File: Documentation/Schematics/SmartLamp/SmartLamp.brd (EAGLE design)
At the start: 53.3 x 51.8 mm, 31 parts, among them J1 POWER_JACKPTH_BREAD, J2 AVR_SPI_PROG_5X2PTH2, Q1 STN4NF03L, Q2 STN4NF03L, Q3 STN4NF03L, U1 MIC2920A, U2 DS3231MZ, U3 ATMEGA8/168/328, U4 HM-10

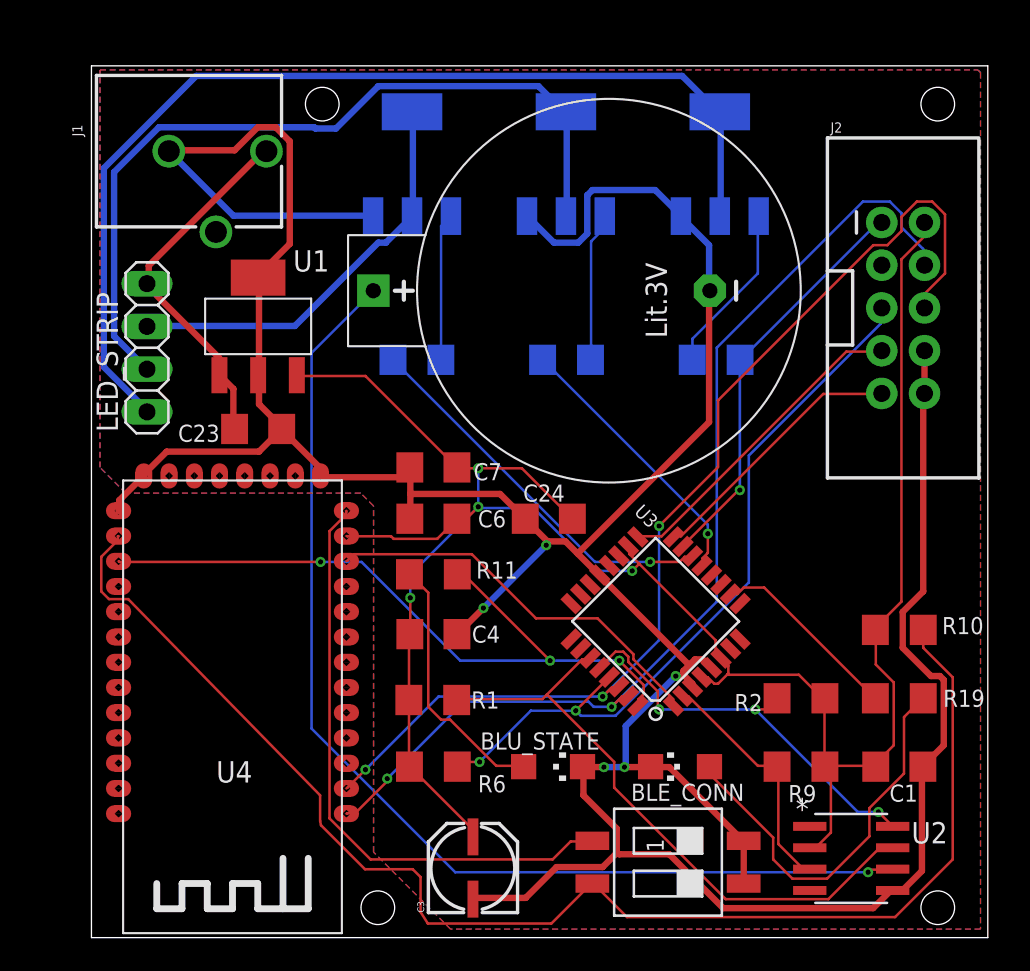
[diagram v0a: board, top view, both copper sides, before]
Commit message: Fixed DC jack and battery holder footprint.. milling level needed for slot holes.
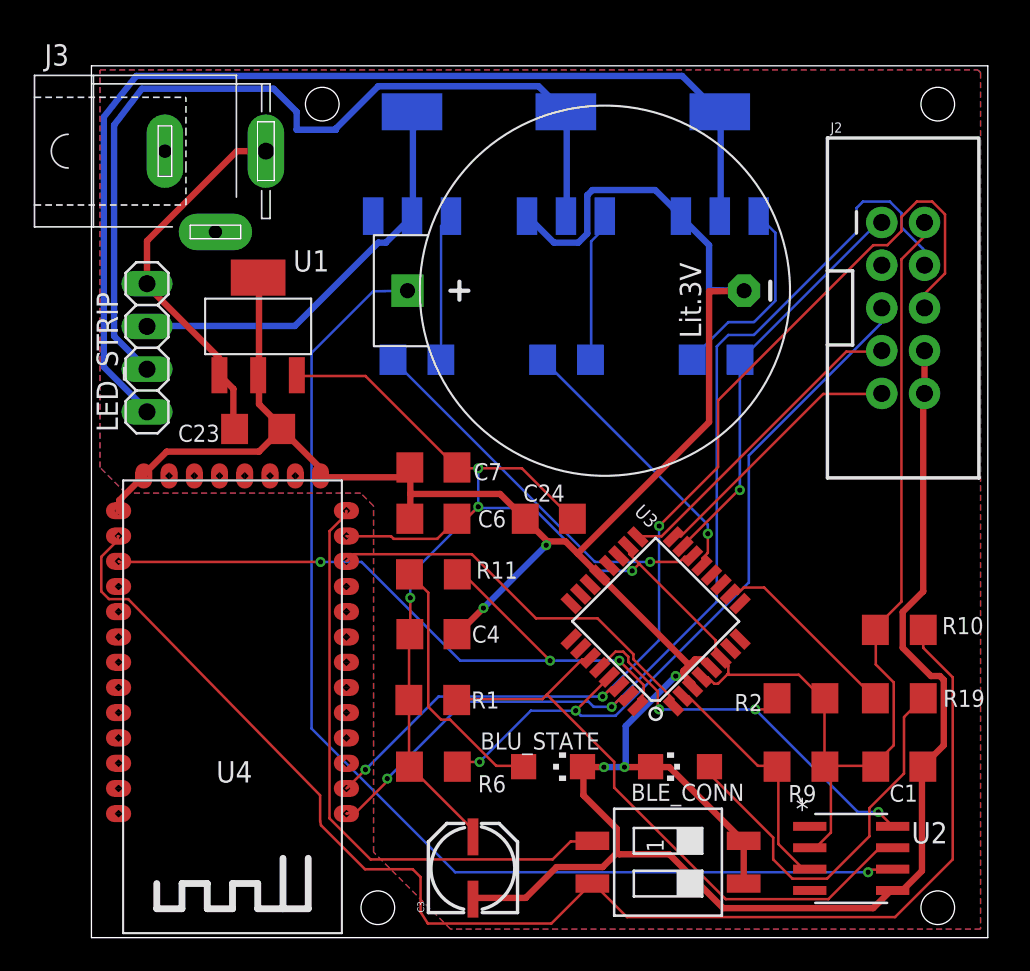
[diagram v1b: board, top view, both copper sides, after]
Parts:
- removed J1: POWER_JACKPTH_BREAD, SparkFun-Connectors:POWER_JACK_PTH_BREAD
- added J3: (no value), con-jack:SPC4077
- G1: value CR2032_EBM -> CR2032AMAZON; device CuSTOM_GB:CR2032_EBM -> CuSTOM_GB:CR2032_AMAZON
- moved G1 2.03 mm to (33.0, 38.4)
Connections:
- net +12V: now also J3.3; no longer J1.PWR
- net GND: now also J3.1; no longer J1.GND
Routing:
- net GND: track 224.4 -> 197.7 mm
- net RED_12V: track 48.4 -> 52.9 mm
- net VBAT: track 65.7 -> 67.7 mm
- net BLUE_12V: track 61.6 -> 63.5 mm
- net N$11: track 10.2 -> 11.9 mm
- net +12V: track 21.7 -> 22.6 mm
- net S_IN: track 62.4 -> 63.3 mm
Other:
- board text added: "SmartLamp SMD v1.1"
- board text removed: "SmartLamp SMD v1.0"

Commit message: Fixed GND - switch connection for HM-10
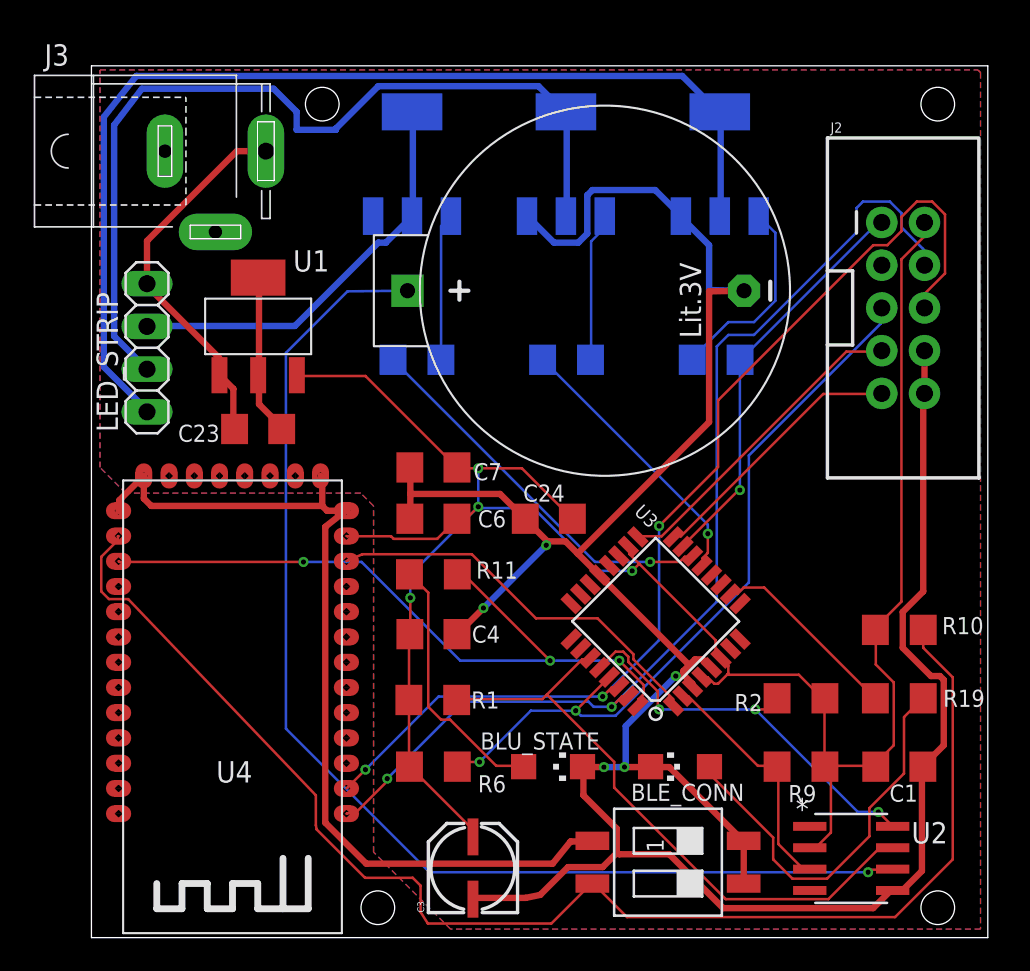
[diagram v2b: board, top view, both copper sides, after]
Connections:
- removed net BLU_SWITCH: S1.1, U4.13
- new net BLU_GND: S1.1, U4.13, U4.14, U4.21, U4.22
- net GND: no longer U4.14, U4.21, U4.22
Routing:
- net BLU_GND: track 0.00 -> 55.0 mm
- net BLU_SWITCH: track 35.8 -> 0.00 mm
- net GND: track 197.7 -> 176.1 mm
- net VBAT: track 67.7 -> 70.7 mm

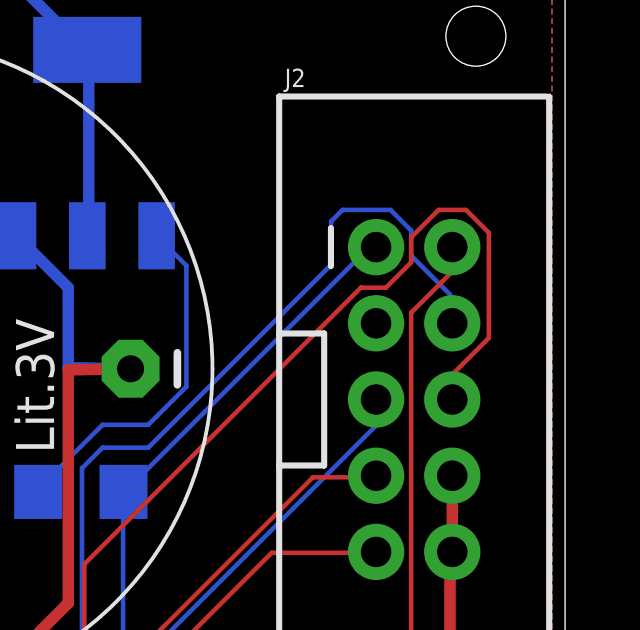
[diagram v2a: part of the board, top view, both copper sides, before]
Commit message: Fixed TX and RX swapped on PCB...
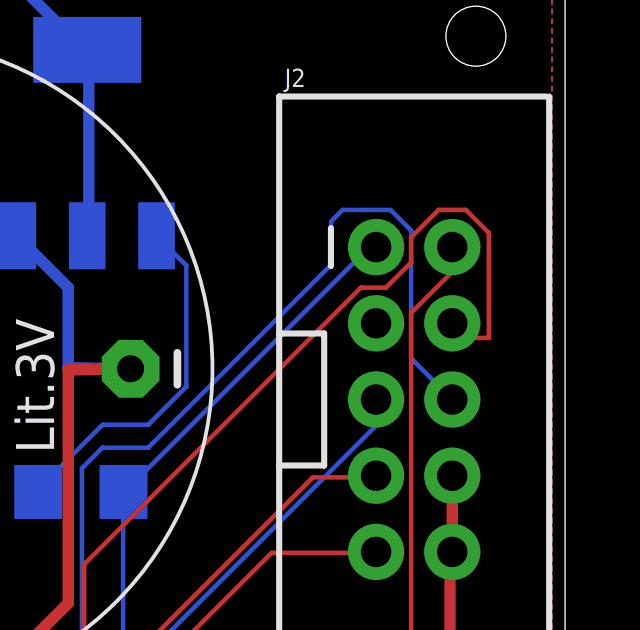
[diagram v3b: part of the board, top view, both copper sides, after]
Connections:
- net S_IN: now also J2.6; no longer J2.4
- net S_OUT: now also J2.4; no longer J2.6
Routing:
- net S_IN: track 63.3 -> 65.9 mm
- net S_OUT: track 64.4 -> 63.5 mm
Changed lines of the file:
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@@
 <contactref element="U4" pad="2"/>
 <contactref element="U3" pad="30"/>
-<contactref element="J2" pad="6"/>
 <wire x1="31.1658" y1="14.859" x2="31.5468" y2="14.859" width="0.1524" layer="1"/>
 <wire x1="30.6324" y1="14.3256" x2="31.1658" y2="14.859" width="0.1524" layer="1"/>
@@
 <wire x1="31.5468" y1="14.859" x2="31.5952" y2="14.91214375" width="0.1524" layer="1"/>
 <wire x1="15.4686" y1="8.9154" x2="15.406" y2="8.866" width="0.1524" layer="1"/>
-<wire x1="49.7586" y1="38.2524" x2="49.7586" y2="37.4904" width="0.1524" layer="1"/>
-<wire x1="50.9778" y1="39.4716" x2="49.7586" y2="38.2524" width="0.1524" layer="1"/>
 <wire x1="50.9778" y1="42.9768" x2="50.9778" y2="39.4716" width="0.1524" layer="1"/>
 <wire x1="50.2158" y1="43.7388" x2="50.9778" y2="42.9768" width="0.1524" layer="1"/>
@@
 <wire x1="33.9852" y1="17.6784" x2="33.9852" y2="24.4602" width="0.1524" layer="16"/>
 <wire x1="30.6324" y1="14.3256" x2="33.9852" y2="17.6784" width="0.1524" layer="16"/>
-<wire x1="49.7586" y1="37.4904" x2="49.758596875" y2="37.41928125" width="0.1524" layer="1"/>
 <via x="30.6324" y="14.3256" extent="1-16" drill="0.3048"/>
 <via x="16.5354" y="9.9822" extent="1-16" drill="0.3048"/>
 <via x="33.9852" y="24.4602" extent="1-16" drill="0.3048"/>
+<contactref element="J2" pad="4"/>
+<wire x1="50.9778" y1="39.4716" x2="49.758596875" y2="39.4716" width="0.1524" layer="1"/>
+<wire x1="49.758596875" y1="39.4716" x2="49.758596875" y2="39.95928125" width="0.1524" layer="1"/>
 </signal>
 <signal name="S_IN">
 <contactref element="U4" pad="1"/>
 <contactref element="U3" pad="31"/>
-<contactref element="J2" pad="4"/>
 <wire x1="31.7754" y1="14.3256" x2="32.1564" y2="14.3256" width="0.1524" layer="1"/>
 <wire x1="31.1658" y1="13.716" x2="31.7754" y2="14.3256" width="0.1524" layer="1"/>
@@
 <wire x1="32.1564" y1="14.3256" x2="32.160884375" y2="14.346459375" width="0.1524" layer="1"/>
 <wire x1="15.4686" y1="7.3914" x2="15.406" y2="7.366" width="0.1524" layer="1"/>
-<wire x1="49.6824" y1="40.9194" x2="49.6824" y2="40.005" width="0.1524" layer="16"/>
-<wire x1="48.387" y1="42.2148" x2="49.6824" y2="40.9194" width="0.1524" layer="16"/>
-<wire x1="48.387" y1="43.053" x2="48.387" y2="42.2148" width="0.1524" layer="16"/>
 <wire x1="47.7012" y1="43.7388" x2="48.387" y2="43.053" width="0.1524" layer="16"/>
 <wire x1="46.101" y1="43.7388" x2="47.7012" y2="43.7388" width="0.1524" layer="16"/>
 <wire x1="37.4142" y1="19.9644" x2="37.4142" y2="35.1282" width="0.1524" layer="16"/>
 <wire x1="31.1658" y1="13.716" x2="37.4142" y2="19.9644" width="0.1524" layer="16"/>
-<wire x1="49.6824" y1="40.005" x2="49.758596875" y2="39.95928125" width="0.1524" layer="16"/>
 <via x="31.1658" y="13.716" extent="1-16" drill="0.3048"/>
 <via x="17.8308" y="9.4488" extent="1-16" drill="0.3048"/>
@@
 <wire x1="45.72" y1="41.91" x2="45.72" y2="43.3578" width="0.1524" layer="16"/>
 <wire x1="45.72" y1="43.3578" x2="46.101" y2="43.7388" width="0.1524" layer="16"/>
+<contactref element="J2" pad="6"/>
+<wire x1="49.758596875" y1="37.41928125" x2="48.387" y2="38.790878125" width="0.1524" layer="16"/>
+<wire x1="48.387" y1="38.790878125" x2="48.387" y2="43.053" width="0.1524" layer="16"/>
 </signal>
 <signal name="N$1">

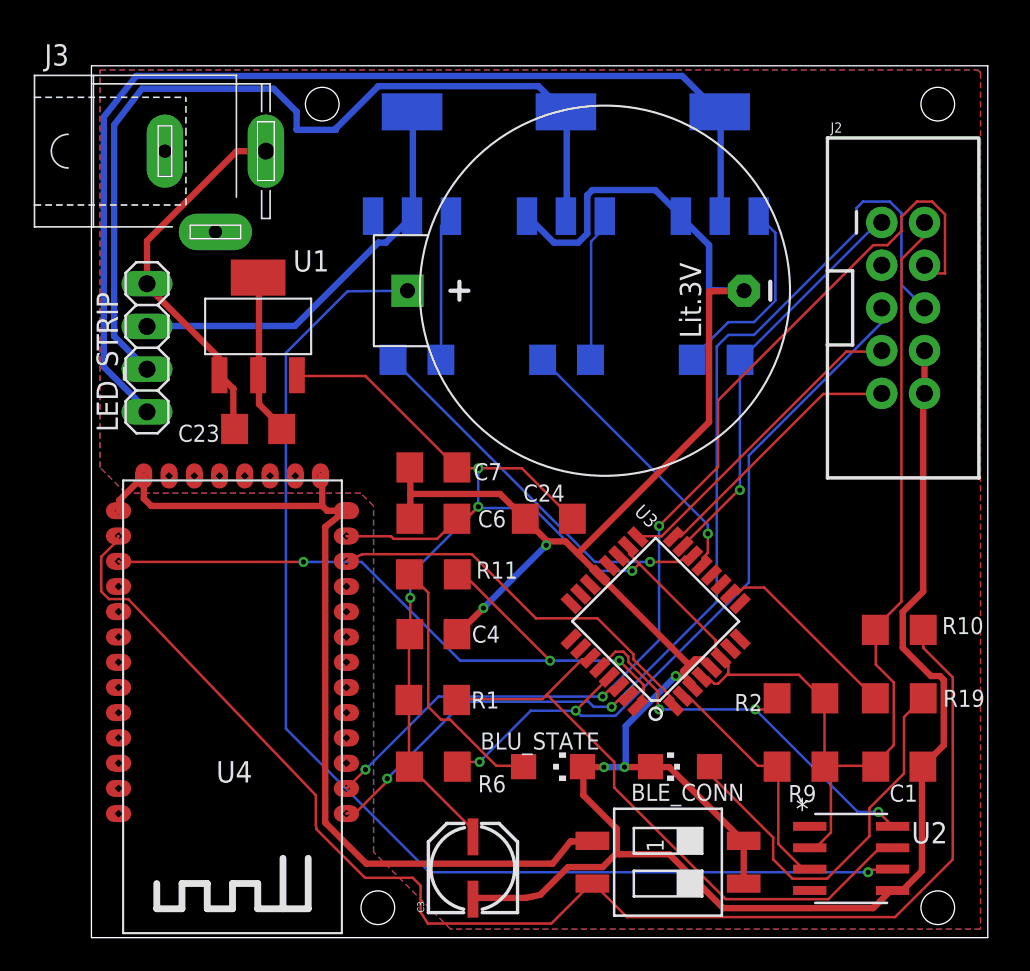
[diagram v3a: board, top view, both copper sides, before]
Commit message: Fixed RX/?TX connection from micro to the BLE module.
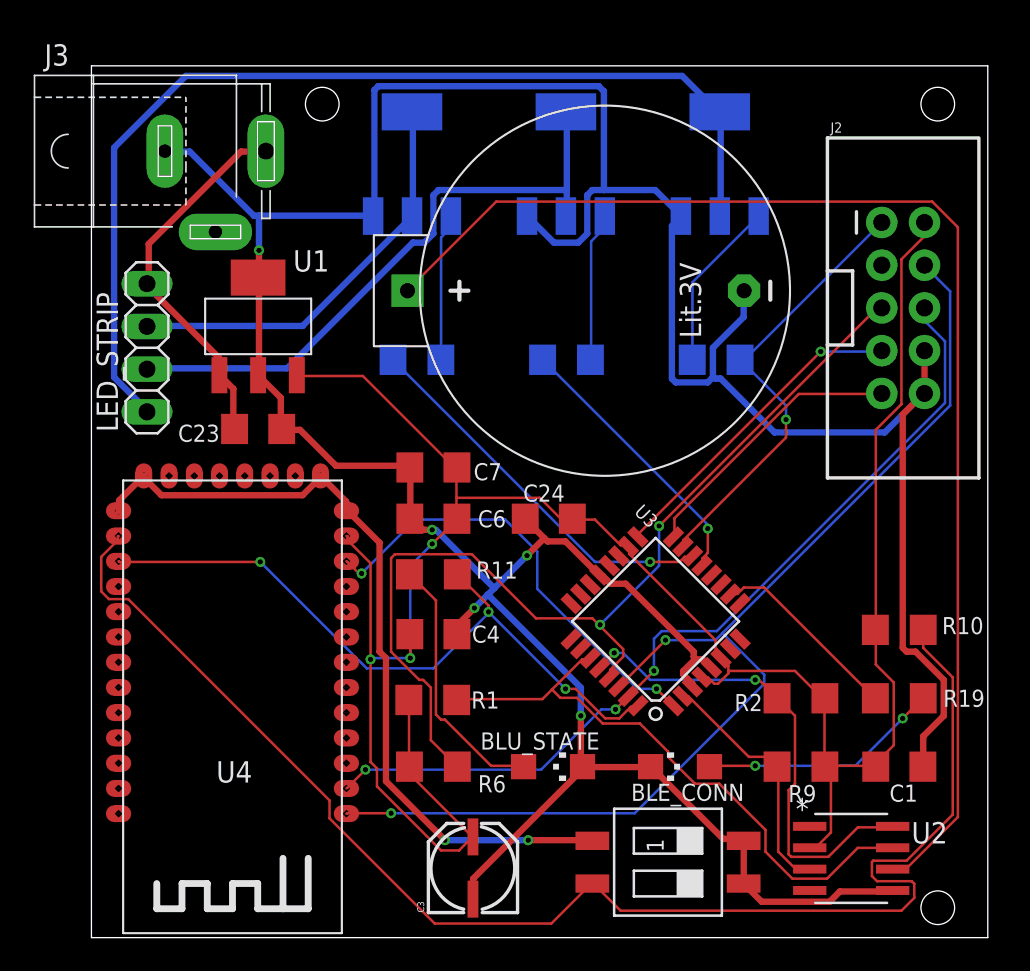
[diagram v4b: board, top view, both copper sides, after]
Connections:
- removed net S_IN: J2.6, U3.31, U4.1
- removed net S_OUT: J2.4, U3.30, U4.2
- new net BLU_RX: J2.6, U3.31, U4.2
- new net BLU_TX: J2.4, U3.30, U4.1
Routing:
- net BLU_TX: track 0.00 -> 67.6 mm, vias 0 -> 2
- net S_IN: track 65.9 -> 0.00 mm, vias 2 -> 0
- net S_OUT: track 63.5 -> 0.00 mm, vias 3 -> 0
- net BLU_RX: track 0.00 -> 52.3 mm, vias 0 -> 3
- net GND: track 176.1 -> 217.9 mm
- net RED_12V: track 52.9 -> 37.0 mm
- net RESET: track 44.5 -> 58.4 mm
- net N$23: track 23.9 -> 14.4 mm, vias 0 -> 2
- net +3V3: track 131.2 -> 138.7 mm, vias 4 -> 3
- net BLU_GND: track 55.0 -> 47.7 mm, vias 0 -> 2
- net VBAT: track 70.7 -> 75.7 mm, vias 1 -> 0
- net SCL: track 24.5 -> 28.9 mm, vias 3 -> 2
- net !BLU_RES: track 23.6 -> 26.9 mm, vias 0 -> 2
- net BLU_KEY: track 82.4 -> 84.8 mm
- net BLU_STATE: track 43.3 -> 40.9 mm
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- removed copper zone on layer 1, net GND
- removed copper zone on layer 16, net GND
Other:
- board text added: "SmartLamp SMD v1.2"
- board text removed: "SmartLamp SMD v1.1"

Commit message: Added micro reset button.
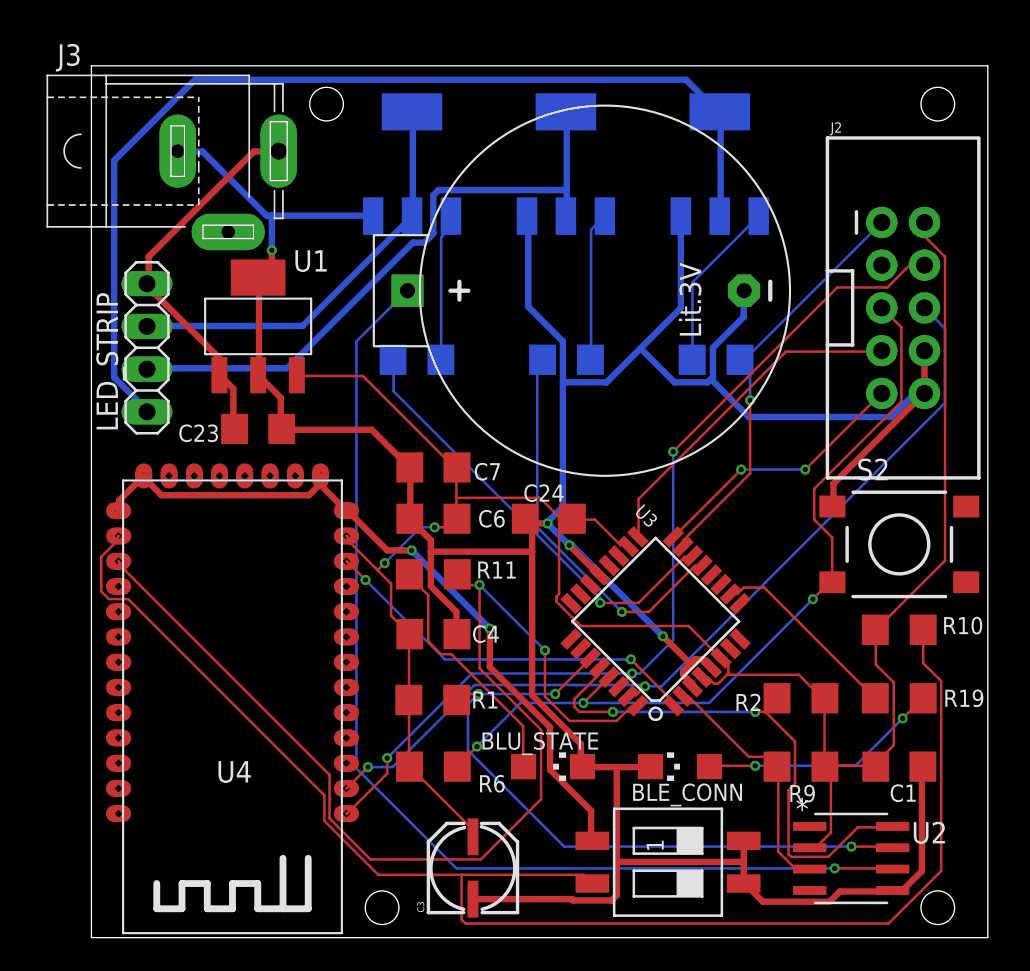
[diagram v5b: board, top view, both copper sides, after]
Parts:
- added S2: DTSM-6, switch-tact:DTSM-6
- moved J3 0.76 mm to (8.38, 46.7)
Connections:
- net GND: now also S2.1
- net RESET: now also S2.3
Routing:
- net BLU_STATE: track 40.9 -> 66.1 mm, vias 3 -> 2
- net VBAT: track 75.7 -> 64.0 mm, vias 0 -> 1
- net BLU_TX: track 67.6 -> 56.1 mm, vias 2 -> 3
- net GND: track 217.9 -> 207.1 mm, vias 5 -> 4
- net +3V3: track 138.7 -> 128.5 mm, vias 3 -> 2
- net RESET: track 58.4 -> 48.4 mm, vias 2 -> 3
- net RED: track 16.4 -> 23.1 mm
- net SDA: track 35.6 -> 40.3 mm, vias 0 -> 3
- net BLU_GND: track 47.7 -> 43.7 mm
- net SCL: track 28.9 -> 32.9 mm
- net !BLU_RES: track 26.9 -> 23.1 mm
- net BLU_KEY: track 84.8 -> 88.3 mm
- net GR: track 22.9 -> 26.2 mm
- net BLUE: track 26.7 -> 24.9 mm
- net SCK: track 19.2 -> 20.4 mm, vias 1 -> 0
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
